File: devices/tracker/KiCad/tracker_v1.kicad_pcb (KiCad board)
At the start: 2 copper layers, 56.5 x 66.8 mm, 45 parts, among them J1 Conn_01x06_Male, J2 Conn_01x09_Male, Q1 AO3401A, U1 STM32L412KB, U2 RFM95W-868S2, U3 ublox_SAM-M8Q, U4 LIS3DH, Y1 32KHz

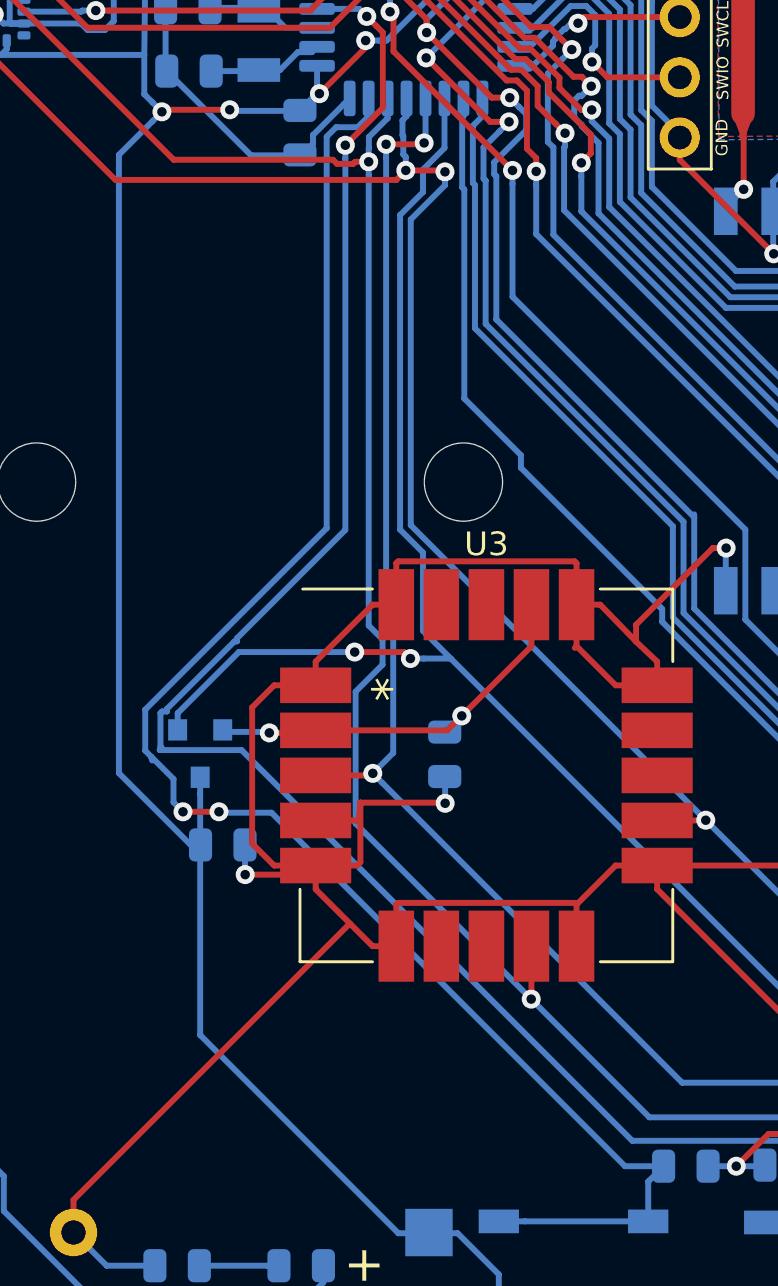
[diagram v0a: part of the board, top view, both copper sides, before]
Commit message: Adding tracker - before class rework
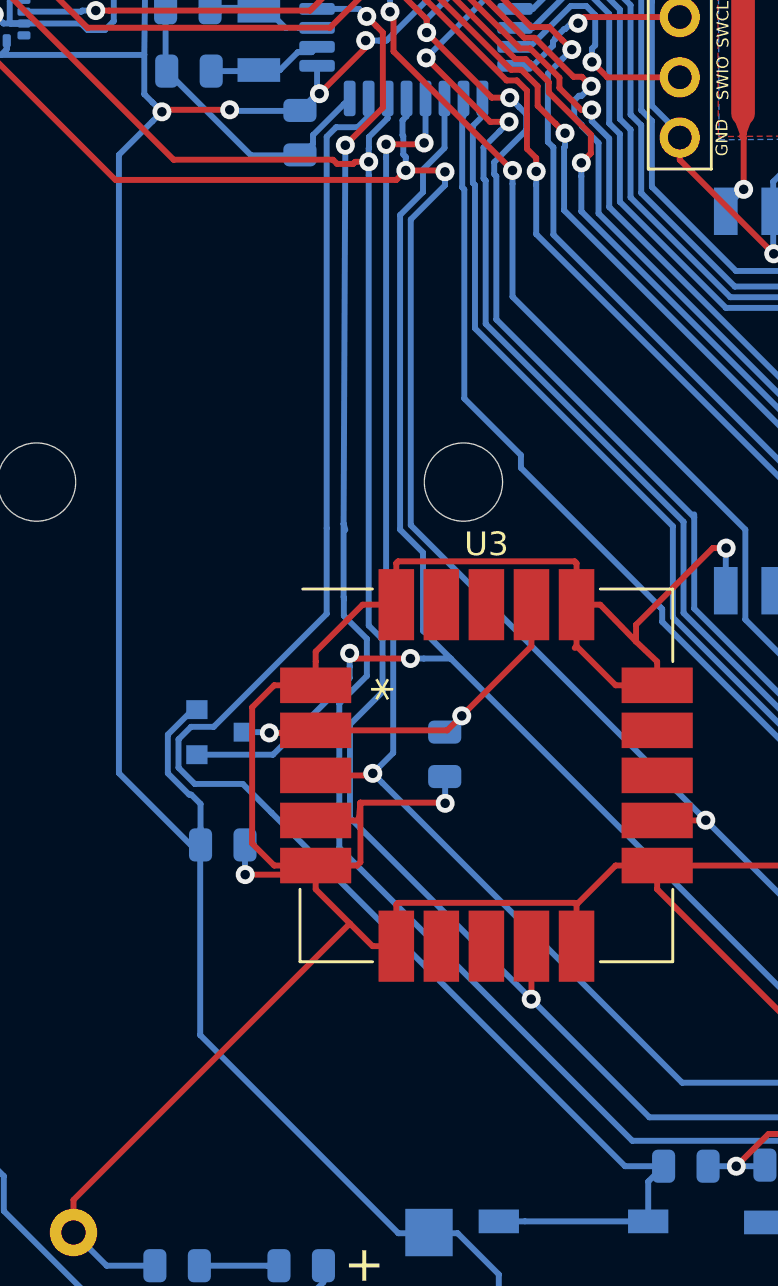
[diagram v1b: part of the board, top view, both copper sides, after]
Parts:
- moved Q1 1.25 mm to (47.1, 65.2), turned to 0 degrees
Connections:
- Q1 pad 2: Net-(C12-Pad2) -> +3V3
- Q1 pad 3: +3V3 -> Net-(C12-Pad2)
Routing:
- net Net-(C4-Pad1): track 82.4 -> 74.9 mm
- net +3V3: track 256.3 -> 260.3 mm
- net Net-(BOOT1-Pad2): track 70.7 -> 68.9 mm, vias 2 -> 0
- net Net-(C12-Pad2): track 17.4 -> 16.7 mm
